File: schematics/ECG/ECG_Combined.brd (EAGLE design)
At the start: 25.4 x 25.4 mm, 78 parts, among them IC1 ADS1293, IC2 LIS3DH, IC3 MCP1703, IC4 CC2541, IC5 FSA4157, IC6 FSA4157, IC7 FSA4157, X1 XTAL-2SMD, X2 XTAL_403, X3 XTAL-CSM7

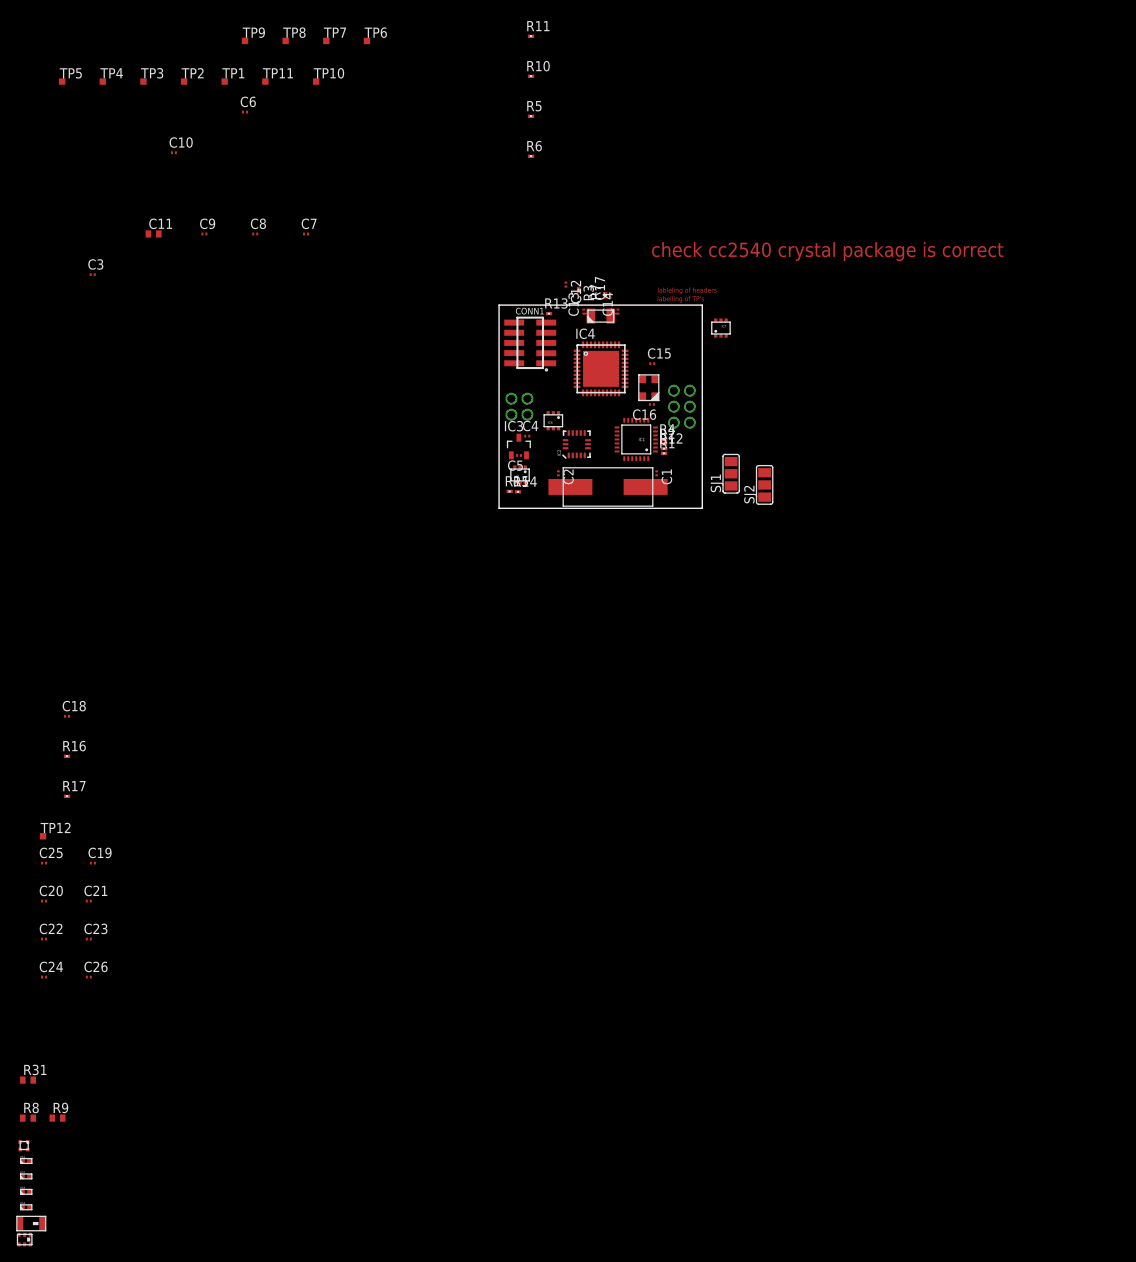
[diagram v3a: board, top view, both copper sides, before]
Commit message: components placed in ideal positions for routing
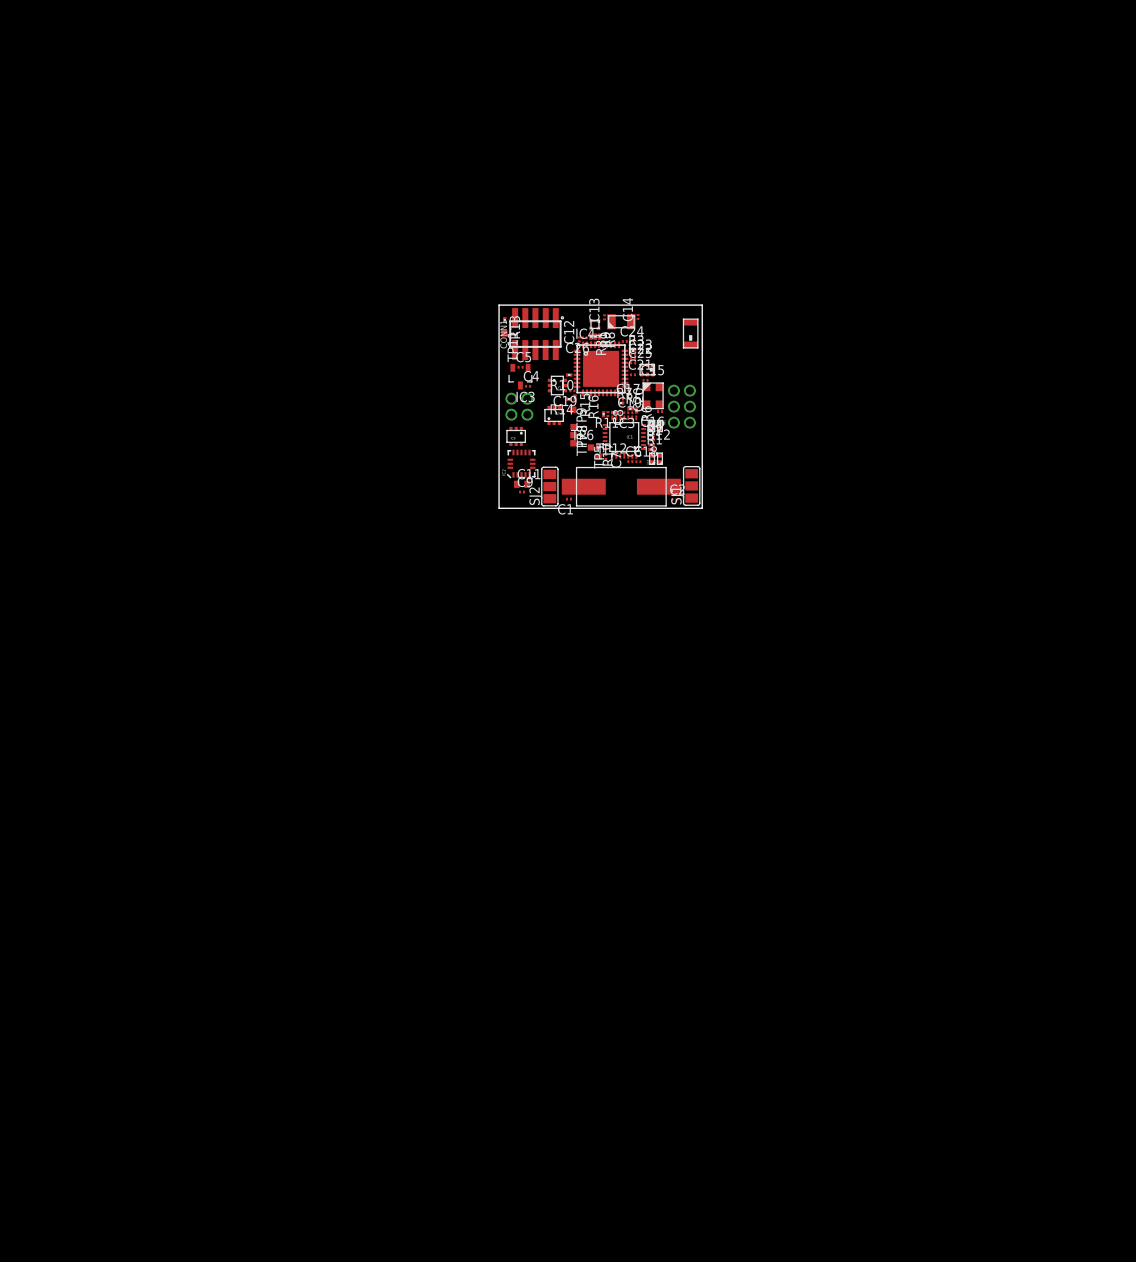
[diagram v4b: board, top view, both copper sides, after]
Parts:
- removed TP1, TP10, TP2, TP3, TP4: TPSTP08SQ, testpad:TP08SQ
- R31, R8, R9: device rcl:R0402 -> rcl:R0201
- moved RF 138.6 mm to (24.0, 21.9), turned to 270 degrees
- moved IC8 133.7 mm to (18.5, 17.3)
- moved TRI_LED 125.0 mm to (12.0, 23.0)
- moved U$2 122.8 mm to (20.1, 10.3), turned to 270 degrees
- moved U$4 122.0 mm to (19.1, 6.20), turned to 90 degrees
- moved U$3 121.1 mm to (20.1, 6.20), turned to 90 degrees
- moved R8 121.0 mm to (12.6, 21.5), turned to 270 degrees
- moved U$1 120.7 mm to (19.2, 10.3), turned to 270 degrees
- moved R9 118.6 mm to (12.0, 21.5), turned to 270 degrees
- moved R31 116.6 mm to (11.5, 21.5), turned to 270 degrees
- moved C24 107.6 mm to (15.7, 20.9)
- moved C22 103.3 mm to (16.8, 18.7)
- moved C26 101.1 mm to (10.7, 21.3), turned to 180 degrees
- moved C23 99.8 mm to (16.8, 19.2)
- moved C20 96.8 mm to (16.1, 14.5), turned to 270 degrees
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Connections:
- removed net BATT_CHECK: IC4.12, IC5.6
- new net BATT_CHECK_SW: IC4.9, IC5.6
- net ALARMB: no longer TP10.TP
- net BATT_SCALED: now also IC4.11; no longer IC4.9
- net BLUE_LED: now also R8.2; no longer R31.2
- net ECG_VCC: now also C18.1, C7.1, C8.1, R11.2, R16.2, R17.2
- net GREEN_LED: now also R31.2; no longer R8.2
- net LA: no longer TP2.TP
- net LL: no longer TP3.TP
- net RA: no longer TP1.TP
- net RL: no longer TP4.TP
- net SPI_SS_ACCEL: now also IC4.12; no longer IC4.11
- net VCC: no longer C18.1, C7.1, C8.1, R11.2, R16.2, R17.2
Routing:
- net P2_4/32K_Q1: track 1.01 -> 0.00 mm
- net P2_3/32K_Q2: track 1.01 -> 0.00 mm
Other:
- board text removed: "check cc2540 crystal package is correct"
- board text removed: "labelling of TP's"
- board text removed: "lableling of headers"

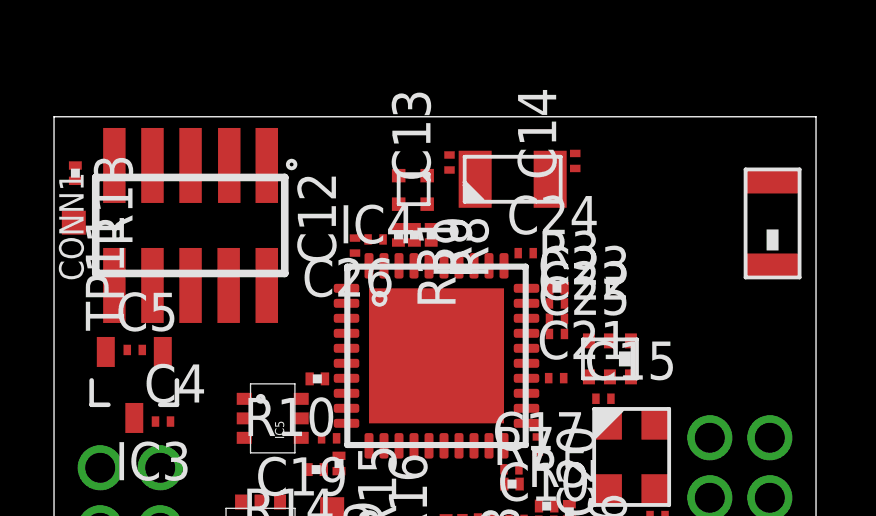
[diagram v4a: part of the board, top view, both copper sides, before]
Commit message: moved cc2541 crystal closer to chip
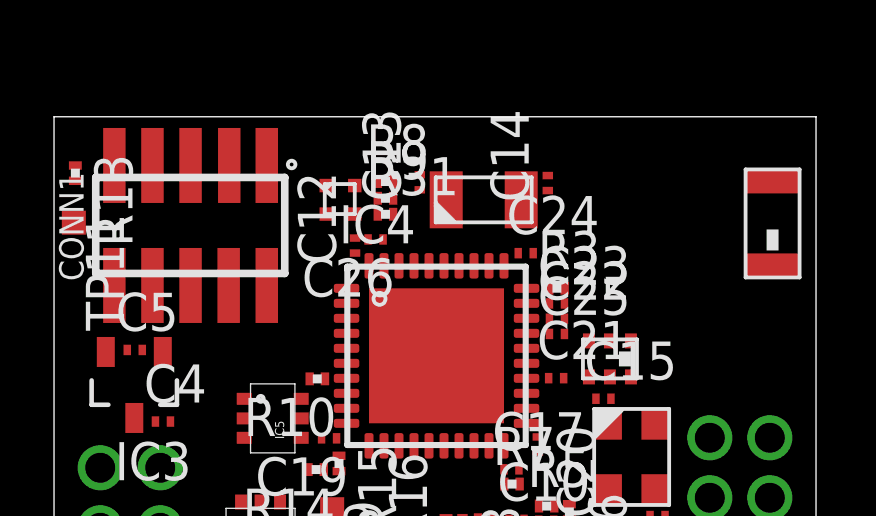
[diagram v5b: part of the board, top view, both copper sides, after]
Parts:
- moved TRI_LED 2.49 mm to (9.53, 22.7), turned to 90 degrees
- moved R8 2.34 mm to (11.0, 23.2), turned to 0 degrees
- moved R9 1.56 mm to (11.0, 22.7), turned to 0 degrees
- moved C13 1.19 mm to (12.2, 23.2)
- moved X1 1.18 mm to (14.3, 22.7)
- moved C14 1.17 mm to (16.5, 23.2)
- moved R31 0.81 mm to (11.0, 22.1), turned to 0 degrees
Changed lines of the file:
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@@
 <attribute name="TP_SIGNAL_NAME" value="" x="-52.6796" y="-7.3406" size="1.778" layer="27" rot="R270" display="off"/>
 </element>
-<element name="C13" library="rcl" package="C0201" value="12pF" x="13.1826" y="23.876" rot="R90"/>
-<element name="C14" library="rcl" package="C0201" value="12pF" x="17.3736" y="23.9268" rot="R90"/>
+<element name="C13" library="rcl" package="C0201" value="12pF" x="12.192" y="23.2156" rot="R90"/>
+<element name="C14" library="rcl" package="C0201" value="12pF" x="16.4592" y="23.1902" rot="R90"/>
 <element name="C15" library="rcl" package="C0201" value="10pF" x="18.3134" y="16.002"/>
 <element name="C16" library="rcl" package="C0201" value="10pF" x="20.1168" y="12.0904" rot="R180"/>
 <element name="X2" library="cts" package="4-SMD" value="XTAL_403" x="19.2544" y="14.0608" rot="R270"/>
-<element name="X1" library="ecs" package="2-SMD" value="XTAL-2SMD" x="15.2884" y="23.3664"/>
+<element name="X1" library="ecs" package="2-SMD" value="XTAL-2SMD" x="14.3232" y="22.6806"/>
 <element name="IC3" library="microchip_regulators" package="SOT23" value="MCP1703" x="2.6758" y="16.46" rot="R180"/>
 <element name="C5" library="rcl" package="C0201" value="1uF" x="2.6924" y="17.6276"/>
@@
 <element name="SJ1" library="jumper" package="SJ_2" value="" x="24.0792" y="2.794" rot="R90"/>
 <element name="SJ2" library="jumper" package="SJ_2" value="" x="6.35" y="2.7178" rot="R90"/>
-<element name="R8" library="rcl" package="R0201" value="1K" x="12.573" y="21.463" rot="R270"/>
-<element name="R31" library="rcl" package="R0201" value="1K" x="11.4808" y="21.463" rot="R270"/>
-<element name="TRI_LED" library="lumex" package="SML-LX0404SIUPGUSB" value="SML-LX0404SIUPGUSB" x="11.9888" y="22.987"/>
-<element name="R9" library="rcl" package="R0201" value="1K" x="12.0142" y="21.463" rot="R270"/>
+<element name="R8" library="rcl" package="R0201" value="1K" x="11.049" y="23.241"/>
+<element name="R31" library="rcl" package="R0201" value="1K" x="11.049" y="22.1488"/>
+<element name="TRI_LED" library="lumex" package="SML-LX0404SIUPGUSB" value="SML-LX0404SIUPGUSB" x="9.525" y="22.6568" rot="R90"/>
+<element name="R9" library="rcl" package="R0201" value="1K" x="11.049" y="22.6822"/>
 <element name="CONN2" library="harwin" package="M80-4-V" value="M80-4V" x="2.54" y="12.7" rot="R180"/>
 <element name="U$1" library="semtech" package="0402" value="ZD_0402" x="19.1516" y="10.287" rot="R270"/>
@@
 <contactref element="IC8" pad="6"/>
 <contactref element="IC8" pad="2"/>
-<wire x1="15.9726" y1="20.8534" x2="17.3736" y2="24.1768" width="0" layer="19" extent="1-1"/>
+<wire x1="15.9726" y1="20.8534" x2="16.4592" y2="23.4402" width="0" layer="19" extent="1-1"/>
 <wire x1="17.019" y1="19.685" x2="15.9726" y2="20.8534" width="0" layer="19" extent="1-1"/>
 <wire x1="17.014" y1="19.177" x2="17.019" y2="19.685" width="0" layer="19" extent="1-1"/>
@@
 <wire x1="20.1168" y1="10.7378" x2="19.1516" y2="10.7378" width="0" layer="19" extent="1-1"/>
 <wire x1="19.8668" y1="12.0904" x2="20.1168" y2="10.7378" width="0" layer="19" extent="1-1"/>
-<wire x1="13.1826" y1="24.126" x2="17.3736" y2="24.1768" width="0" layer="19" extent="1-1"/>
-<wire x1="10.4688" y1="21.3106" x2="13.1826" y2="24.126" width="0" layer="19" extent="1-1"/>
+<wire x1="12.192" y1="23.4656" x2="16.4592" y2="23.4402" width="0" layer="19" extent="1-1"/>
+<wire x1="10.4688" y1="21.3106" x2="12.192" y2="23.4656" width="0" layer="19" extent="1-1"/>
 <wire x1="10.033" y1="21.3574" x2="10.4688" y2="21.3106" width="0" layer="19" extent="1-1"/>
 <wire x1="9.7498" y1="19.6812" x2="10.033" y2="21.3574" width="0" layer="19" extent="1-1"/>
@@
 <wire x1="15.7498" y1="15.1812" x2="15.7498" y2="16.6812" width="0" layer="19" extent="1-1"/>
 <wire x1="16.129" y1="14.728" x2="15.7498" y2="15.1812" width="0" layer="19" extent="1-1"/>
-<wire x1="12.4388" y1="23.437" x2="14.9998" y2="20.4312" width="0" layer="19" extent="1-1"/>
-<wire x1="10.9688" y1="21.3106" x2="12.4388" y2="23.437" width="0" layer="19" extent="1-1"/>
+<wire x1="9.075" y1="23.1068" x2="14.9998" y2="20.4312" width="0" layer="19" extent="1-1"/>
+<wire x1="10.9688" y1="21.3106" x2="9.075" y2="23.1068" width="0" layer="19" extent="1-1"/>
 <wire x1="10.9998" y1="20.4312" x2="10.9688" y2="21.3106" width="0" layer="19" extent="1-1"/>
 <wire x1="7.0914" y1="19.777" x2="10.9998" y2="20.4312" width="0" layer="19" extent="1-1"/>
@@
 <contactref element="C13" pad="1"/>
 <contactref element="X1" pad="1"/>
-<wire x1="14.0384" y1="23.3164" x2="13.1826" y2="23.626" width="0" layer="19" extent="1-1"/>
-<wire x1="13.9998" y1="20.4312" x2="14.0384" y2="23.3164" width="0" layer="19" extent="1-1"/>
+<wire x1="13.0732" y1="22.6306" x2="12.192" y2="22.9656" width="0" layer="19" extent="1-1"/>
+<wire x1="13.9998" y1="20.4312" x2="13.0732" y2="22.6306" width="0" layer="19" extent="1-1"/>
 </signal>
 <signal name="P2_4/32K_Q1">
@@
 <contactref element="C14" pad="1"/>
 <contactref element="X1" pad="2"/>
-<wire x1="16.5384" y1="23.3164" x2="17.3736" y2="23.6768" width="0" layer="19" extent="1-1"/>
-<wire x1="14.4998" y1="20.4312" x2="16.5384" y2="23.3164" width="0" layer="19" extent="1-1"/>
+<wire x1="15.5732" y1="22.6306" x2="16.4592" y2="22.9402" width="0" layer="19" extent="1-1"/>
+<wire x1="14.4998" y1="20.4312" x2="15.5732" y2="22.6306" width="0" layer="19" extent="1-1"/>
 </signal>
 <signal name="XOSC_Q1">
@@
 <contactref element="IC4" pad="36"/>
 <contactref element="R8" pad="2"/>
-<wire x1="12.573" y1="21.208" x2="12.4998" y2="20.4312" width="0" layer="19" extent="1-1"/>
+<wire x1="11.304" y1="23.241" x2="12.4998" y2="20.4312" width="0" layer="19" extent="1-1"/>
 </signal>
 <signal name="GREEN_LED">
 <contactref element="IC4" pad="38"/>
 <contactref element="R31" pad="2"/>
-<wire x1="11.4808" y1="21.208" x2="11.4998" y2="20.4312" width="0" layer="19" extent="1-1"/>
+<wire x1="11.304" y1="22.1488" x2="11.4998" y2="20.4312" width="0" layer="19" extent="1-1"/>
 </signal>
 <signal name="N$3">
 <contactref element="TRI_LED" pad="3"/>
 <contactref element="R9" pad="1"/>
-<wire x1="12.0142" y1="21.718" x2="11.4888" y2="22.487" width="0" layer="19" extent="1-1"/>
+<wire x1="10.794" y1="22.6822" x2="10.025" y2="22.1568" width="0" layer="19" extent="1-1"/>
 </signal>
 <signal name="N$9">
 <contactref element="TRI_LED" pad="4"/>
 <contactref element="R31" pad="1"/>
-<wire x1="11.4808" y1="21.718" x2="11.4888" y2="23.437" width="0" layer="19" extent="1-1"/>
+<wire x1="10.794" y1="22.1488" x2="9.075" y2="22.1568" width="0" layer="19" extent="1-1"/>
 </signal>
 <signal name="N$20">
 <contactref element="TRI_LED" pad="2"/>
 <contactref element="R8" pad="1"/>
-<wire x1="12.573" y1="21.718" x2="12.4388" y2="22.487" width="0" layer="19" extent="1-1"/>
+<wire x1="10.794" y1="23.241" x2="10.025" y2="23.1068" width="0" layer="19" extent="1-1"/>
 </signal>
 <signal name="RED_LED">
 <contactref element="R9" pad="2"/>
 <contactref element="IC4" pad="37"/>
-<wire x1="11.9998" y1="20.4312" x2="12.0142" y2="21.208" width="0" layer="19" extent="1-1"/>
+<wire x1="11.9998" y1="20.4312" x2="11.304" y2="22.6822" width="0" layer="19" extent="1-1"/>
 </signal>
 <signal name="N$6">

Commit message: continued routing
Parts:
- removed R13: 0, rcl:R0201
- removed SJ1, SJ2: (no value), jumper:SJ_2
- removed TP11: TPSTP08SQ, testpad:TP08SQ
- added U$5: TC2030-MCP-NL, tagconnect:TC2030-MCP-NL
- moved RF 5.03 mm to (23.2, 16.9), turned to 180 degrees
- moved U$3 3.62 mm to (23.4, 7.67)
- moved C2 3.56 mm to (21.0, 4.50), turned to 90 degrees
- moved C1 3.35 mm to (8.79, 4.50), turned to 90 degrees
- moved U$4 2.85 mm to (21.8, 7.19)
- moved C5 1.53 mm to (1.96, 16.3), turned to 90 degrees
- moved X1 1.45 mm to (14.4, 24.1)
- moved TP9 1.44 mm to (10.3, 11.3)
- moved C13 1.43 mm to (12.0, 24.6)
- moved C11 1.43 mm to (2.97, 1.57)
- moved R3 1.41 mm to (16.6, 21.1), turned to 90 degrees
- moved C9 1.40 mm to (2.97, 0.64)
- moved C26 1.16 mm to (9.58, 21.1)
- moved R17 1.14 mm to (11.2, 7.64)
- moved C12 1.14 mm to (9.14, 20.4), turned to 270 degrees
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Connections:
- removed net N$1: CONN1.9, R13.1
- removed net N$10: C2.2, SJ1.2
- removed net N$13: C1.2, SJ2.2
- removed net N$2: R13.2, TP11.TP
- net ECG_VCC: now also C1.2, C2.2
- net GND: now also U$5.1; no longer SJ1.3, SJ2.3
- net P2_1/DD: now also U$5.5
- net P2_2/DC: now also U$5.2
- net RESET_N: now also U$5.3
- net VCC: now also U$5.4; no longer SJ1.1, SJ2.1
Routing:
- net VCC: track 0.00 -> 64.9 mm, vias 0 -> 9
- net GND: track 0.00 -> 43.8 mm, vias 0 -> 19
- net P2_1/DD: track 0.00 -> 23.9 mm, vias 0 -> 3
- net P2_2/DC: track 0.00 -> 23.7 mm, vias 0 -> 3
- net SPI_CLK: track 0.00 -> 16.8 mm, vias 0 -> 2
- net ECG_VCC: track 0.00 -> 14.7 mm, vias 0 -> 1
- net RESET_N: track 0.00 -> 13.7 mm, vias 0 -> 2
- net ACCEL_VCC: track 0.00 -> 11.6 mm
- net SPI_MOSI: track 0.00 -> 10.3 mm, vias 0 -> 2
- net SPI_MISO: track 0.00 -> 9.33 mm
- net XTAL1: track 0.00 -> 9.08 mm
- net XTAL2: track 0.00 -> 9.05 mm
- net XOSC_Q2: track 0.00 -> 6.94 mm
- net ACCEL_INT1: track 0.00 -> 6.52 mm
- net SPI_SS: track 0.00 -> 6.22 mm
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- added copper zone on layer 16, net GND
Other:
- board size 25.4 x 25.4 mm -> 25.7 x 25.7 mm
